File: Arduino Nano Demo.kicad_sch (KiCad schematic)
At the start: 26 parts, among them J1 Barrel_Jack, J2 Conn_01x01_Female, J3 Conn_01x01_Female, P1 Digital, P2 Analog, P3 CONN_01X01, P4 CONN_01X01, P5 CONN_01X01, P6 CONN_01X01, SW1 SW_SPST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

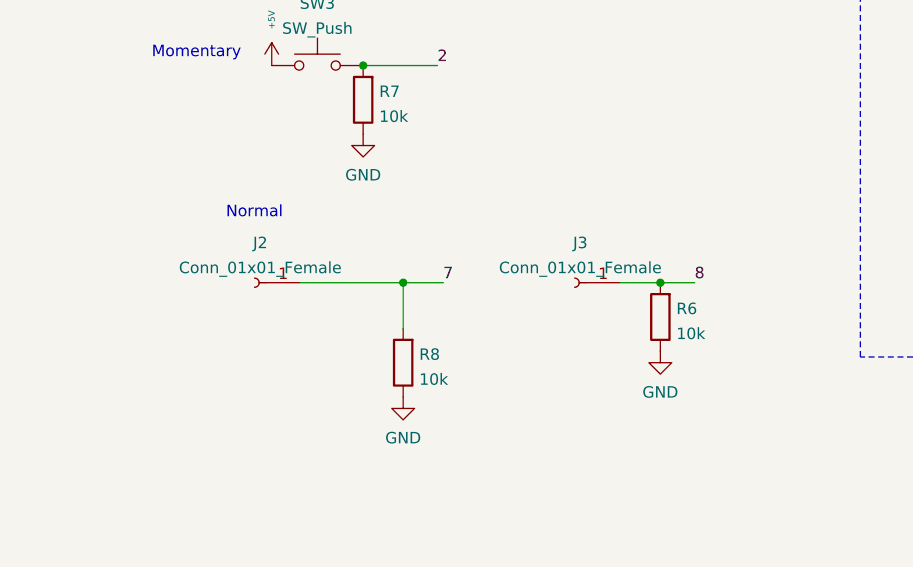
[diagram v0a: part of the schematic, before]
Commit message: Added JST connectors
Found some nice JST plugs to add for the inputs; makes more sense to have grounds for them anyway. Cool 3D models and everything.
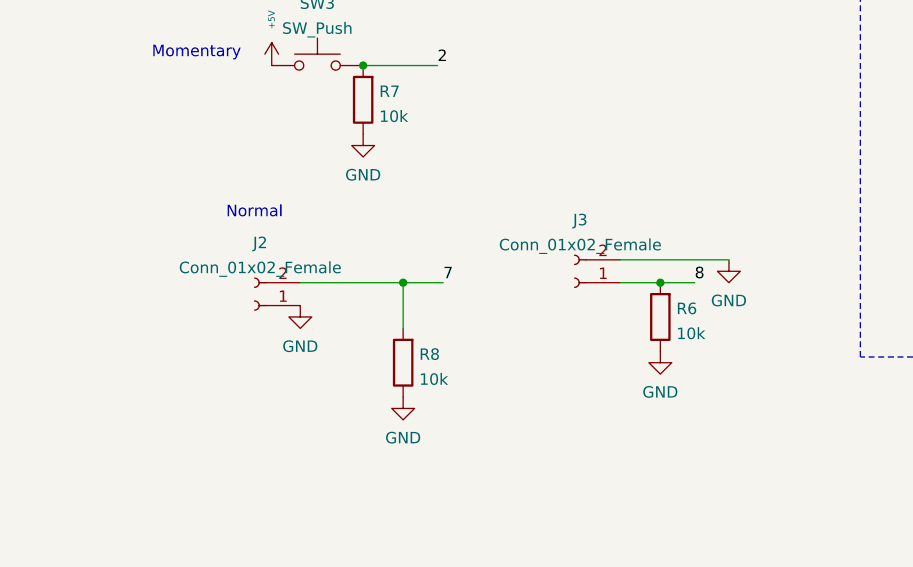
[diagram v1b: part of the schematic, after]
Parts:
- removed J2, J3: Conn_01x01_Female, Connector_PinHeader_2.54mm:PinHeader_1x01_P2.54mm_Vertical, symbol Connector:Conn_01x01_Female
- added J2, J3: Conn_01x02_Female, Connector_JST:JST_EH_B2B-EH-A_1x02_P2.50mm_Vertical, symbol Connector:Conn_01x02_Female
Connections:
- net 7: now also J2.2 (Pin_2)
- net 8: now also J3.1 (Pin_1)
- net GND: now also J2.1 (Pin_1), J3.2 (Pin_2)
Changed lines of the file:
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@@
     (stroke (width 0) (type solid) (color 0 0 0 0))
+  )
+  (wire (pts (xy 187.96 61.595) (xy 200.025 61.595))
+    (stroke (width 0) (type default) (color 0 0 0 0))
   )
   (wire (pts (xy 267.97 40.64) (xy 257.81 40.64))
@@
     (pin "1")
   )
+  (symbol (lib_id "Connector:Conn_01x02_Female") (at 147.32 66.675 180) (unit 1)
+    (in_bom yes) (on_board yes) (fields_autoplaced)
+    (property "Reference" "J2" (id 0) (at 147.955 59.7113 0))
+    (property "Value" "Conn_01x02_Female" (id 1) (at 147.955 62.4864 0))
+    (property "Footprint" "Connector_JST:JST_EH_B2B-EH-A_1x02_P2.50mm_Vertical" (id 2) (at 147.32 66.675 0)
+      (effects (font (size 1.27 1.27)) hide)
+    )
+    (property "Datasheet" "~" (id 3) (at 147.32 66.675 0)
+      (effects (font (size 1.27 1.27)) hide)
+    )
+    (pin "1")
+    (pin "2")
+  )
   (symbol (lib_id "power:GND") (at 43.18 36.83 0) (unit 1)
     (in_bom yes) (on_board yes) (fields_autoplaced)
@@
     (pin "2")
   )
-  (symbol (lib_id "Connector:Conn_01x01_Female") (at 147.32 64.135 180) (unit 1)
-    (in_bom yes) (on_board yes) (fields_autoplaced)
-    (property "Reference" "J2" (id 0) (at 147.955 59.7113 0))
-    (property "Value" "Conn_01x01_Female" (id 1) (at 147.955 62.4864 0))
-    (property "Footprint" "Connector_PinHeader_2.54mm:PinHeader_1x01_P2.54mm_Vertical" (id 2) (at 147.32 64.135 0)
-      (effects (font (size 1.27 1.27)) hide)
-    )
-    (property "Datasheet" "~" (id 3) (at 147.32 64.135 0)
+  (symbol (lib_id "power:GND") (at 200.025 61.595 0) (unit 1)
+    (in_bom yes) (on_board yes) (fields_autoplaced)
+    (property "Reference" "#PWR0103" (id 0) (at 200.025 67.945 0)
+      (effects (font (size 1.27 1.27)) hide)
+    )
+    (property "Value" "GND" (id 1) (at 200.025 66.1575 0))
+    (property "Footprint" "" (id 2) (at 200.025 61.595 0)
+      (effects (font (size 1.27 1.27)) hide)
+    )
+    (property "Datasheet" "" (id 3) (at 200.025 61.595 0)
       (effects (font (size 1.27 1.27)) hide)
     )
@@
     (pin "2")
   )
-  (symbol (lib_id "Connector:Conn_01x01_Female") (at 182.88 64.135 180) (unit 1)
-    (in_bom yes) (on_board yes) (fields_autoplaced)
-    (property "Reference" "J3" (id 0) (at 183.515 59.7113 0))
-    (property "Value" "Conn_01x01_Female" (id 1) (at 183.515 62.4864 0))
-    (property "Footprint" "Connector_PinHeader_2.54mm:PinHeader_1x01_P2.54mm_Vertical" (id 2) (at 182.88 64.135 0)
+  (symbol (lib_id "Connector:Conn_01x02_Female") (at 182.88 64.135 180) (unit 1)
+    (in_bom yes) (on_board yes) (fields_autoplaced)
+    (property "Reference" "J3" (id 0) (at 183.515 57.1713 0))
+    (property "Value" "Conn_01x02_Female" (id 1) (at 183.515 59.9464 0))
+    (property "Footprint" "Connector_JST:JST_EH_B2B-EH-A_1x02_P2.50mm_Vertical" (id 2) (at 182.88 64.135 0)
       (effects (font (size 1.27 1.27)) hide)
     )
@@
     )
     (pin "1")
+    (pin "2")
   )
   (symbol (lib_id "power:GND") (at 151.13 129.54 0) (unit 1)
@@
     (pin "2")
   )
+  (symbol (lib_id "power:GND") (at 152.4 66.675 0) (unit 1)
+    (in_bom yes) (on_board yes) (fields_autoplaced)
+    (property "Reference" "#PWR0102" (id 0) (at 152.4 73.025 0)
+      (effects (font (size 1.27 1.27)) hide)
+    )
+    (property "Value" "GND" (id 1) (at 152.4 71.2375 0))
+    (property "Footprint" "" (id 2) (at 152.4 66.675 0)
+      (effects (font (size 1.27 1.27)) hide)
+    )
+    (property "Datasheet" "" (id 3) (at 152.4 66.675 0)
+      (effects (font (size 1.27 1.27)) hide)
+    )
+    (pin "1")
+  )
   (symbol (lib_id "Device:R") (at 151.13 114.3 0) (unit 1)
     (in_bom yes) (on_board yes) (fields_autoplaced)
@@
       (reference "#PWR0101") (unit 1) (value "GND") (footprint "")
     )
+    (path "/cf05bfeb-e5d8-4512-b8f2-71136447f021"
+      (reference "#PWR0102") (unit 1) (value "GND") (footprint "")
+    )
+    (path "/2797c7d4-d5fc-458b-bda2-79ab1f8f480d"
+      (reference "#PWR0103") (unit 1) (value "GND") (footprint "")
+    )
     (path "/6bf6bd0c-5031-4418-9b41-b2c0bc312ed1"
       (reference "D1") (unit 1) (value "LED") (footprint "LED_THT:LED_D5.0mm")
@@
       (reference "J1") (unit 1) (value "Barrel_Jack") (footprint "Connector_BarrelJack:BarrelJack_CUI_PJ-063AH_Horizontal")
     )
-    (path "/2c0f207c-b80e-4d6b-9ec3-481ad8827f44"
-      (reference "J2") (unit 1) (value "Conn_01x01_Female") (footprint "Connector_PinHeader_2.54mm:PinHeader_1x01_P2.54mm_Vertical")
-    )
-    (path "/b6baee3f-9d6c-4256-afdd-f7ec59c8a6a2"
-      (reference "J3") (unit 1) (value "Conn_01x01_Female") (footprint "Connector_PinHeader_2.54mm:PinHeader_1x01_P2.54mm_Vertical")
+    (path "/079a791d-4be3-4f64-b2b4-2689af465fb0"
+      (reference "J2") (unit 1) (value "Conn_01x02_Female") (footprint "Connector_JST:JST_EH_B2B-EH-A_1x02_P2.50mm_Vertical")
+    )
+    (path "/b0ec37f7-0025-4994-8d10-d24e8e471c8e"
+      (reference "J3") (unit 1) (value "Conn_01x02_Female") (footprint "Connector_JST:JST_EH_B2B-EH-A_1x02_P2.50mm_Vertical")
     )
     (path "/00000000-0000-0000-0000-000056d73fac"

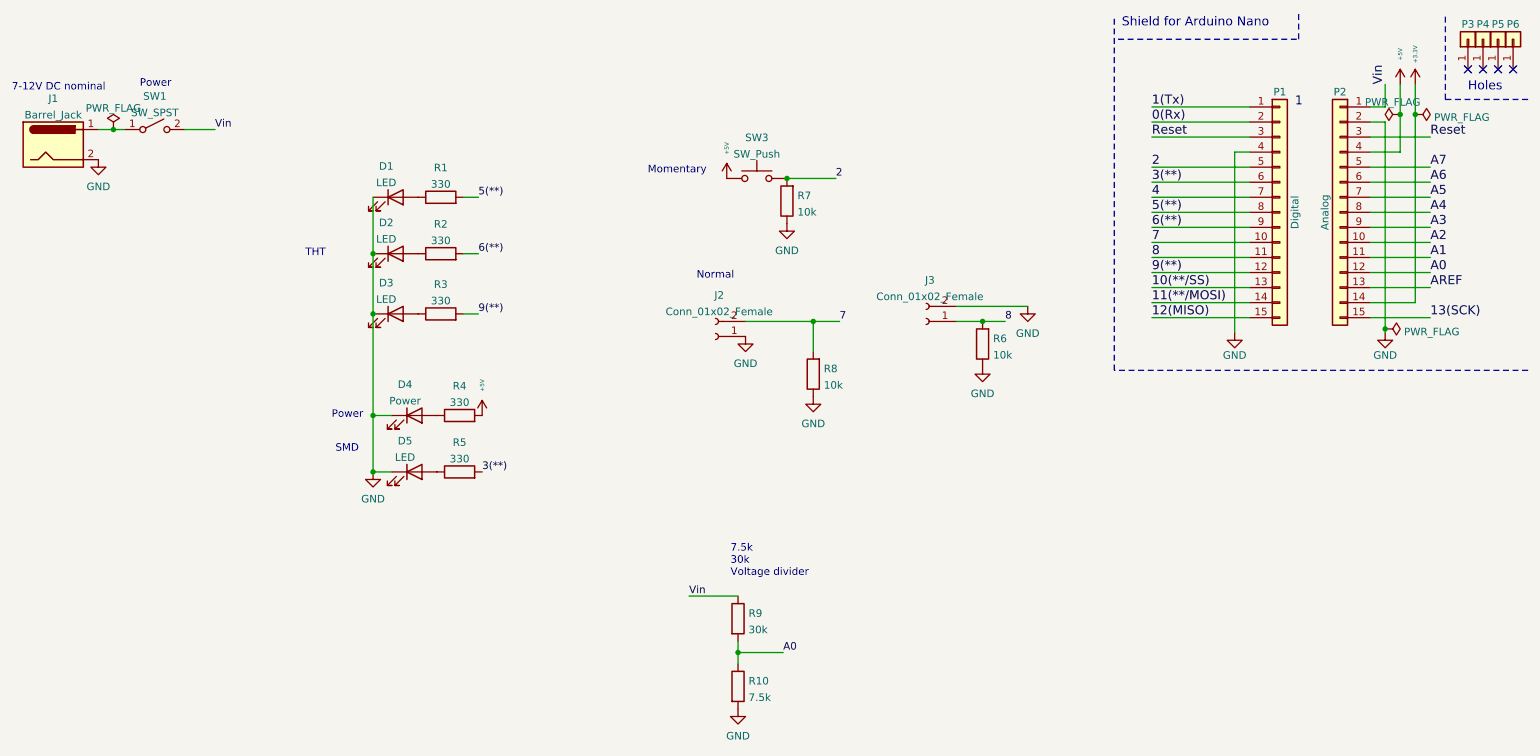
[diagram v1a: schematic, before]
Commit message: Minor Tweaks
Based on feedback I tweaked the example schematic a little bit; all formatting/positioning stuff --- no real changes
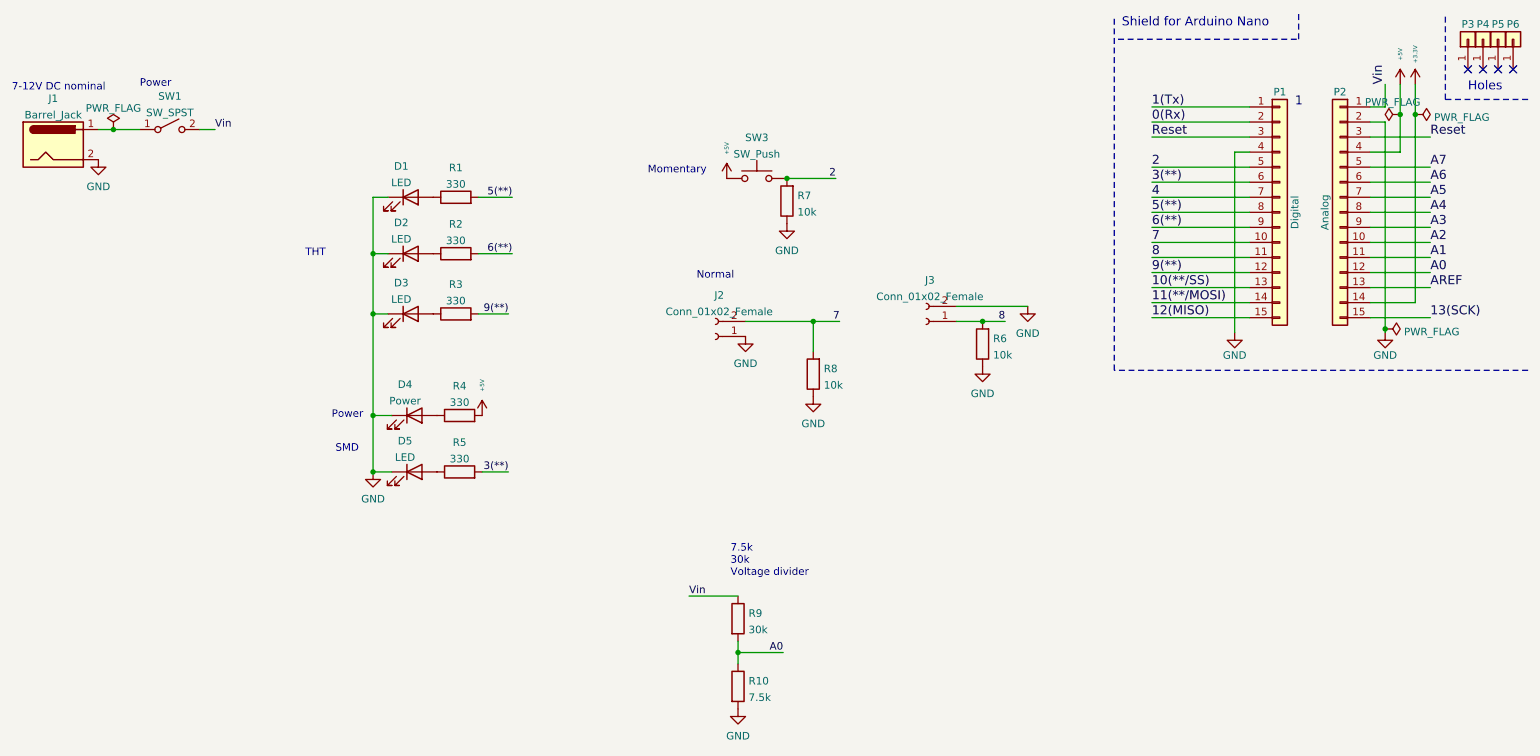
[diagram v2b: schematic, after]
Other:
- moved on the sheet: D1, D2, D3, R1, R2, R3, SW1
